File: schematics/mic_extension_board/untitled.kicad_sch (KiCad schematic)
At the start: 10 parts, among them J9 Conn_01x03_Female, U10 LM4881M/NOPB

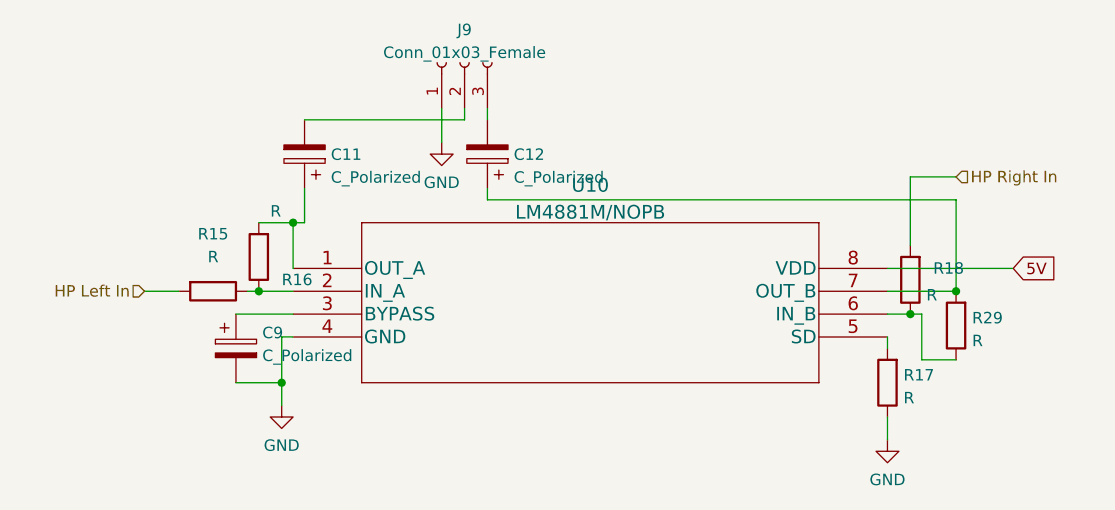
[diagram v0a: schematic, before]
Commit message: re-added component values previously lost due to kicad mishap
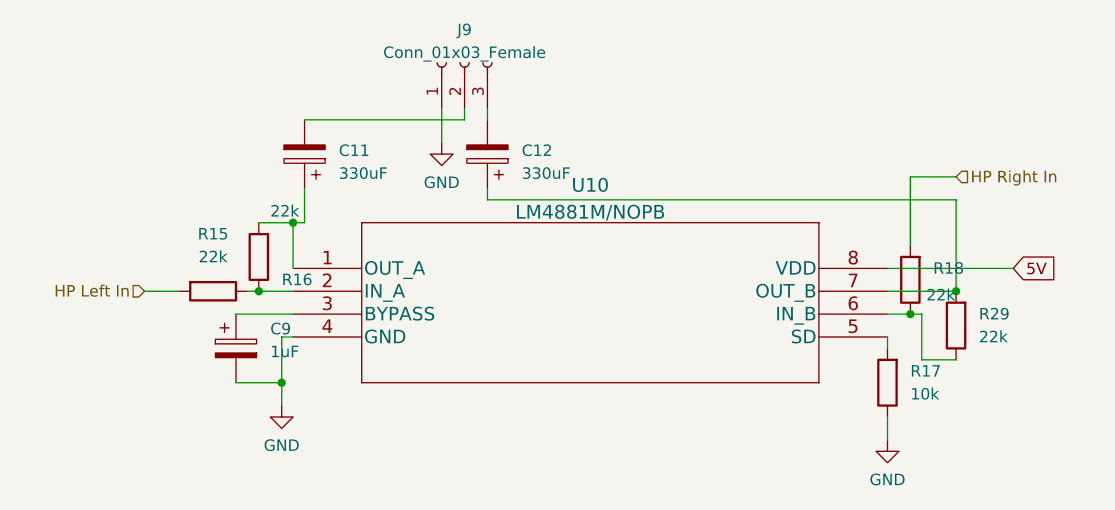
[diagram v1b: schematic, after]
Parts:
- C11, C12: value C_Polarized -> 330uF
- C9: value C_Polarized -> 1uF
- R15, R16, R18, R29: value R -> 22k
- R17: value R -> 10k
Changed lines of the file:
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@@
       (effects (font (size 1.27 1.27)))
     )
-    (property "Value" "R" (at 95.25 55.88 90)
+    (property "Value" "22k" (at 95.25 55.88 90)
       (effects (font (size 1.27 1.27)))
     )
@@
       (effects (font (size 1.27 1.27)) (justify right))
     )
-    (property "Value" "R" (at 174.498 60.1222 0)
+    (property "Value" "22k" (at 174.498 60.1222 0)
       (effects (font (size 1.27 1.27)) (justify right))
     )
@@
       (effects (font (size 1.27 1.27)) (justify right))
     )
-    (property "Value" "R" (at 101.6 50.8 0)
+    (property "Value" "22k" (at 101.6 50.8 0)
       (effects (font (size 1.27 1.27)) (justify right))
     )
@@
   (symbol (lib_id "Device:R") (at 170.18 69.85 180) (unit 1)
     (in_bom yes) (on_board yes) (dnp no) (fields_autoplaced)
-    (property "Reference" "R17" (at 171.958 69.0153 0)
-      (effects (font (size 1.27 1.27)) (justify right))
-    )
-    (property "Value" "R" (at 171.958 71.5522 0)
+    (property "Reference" "R17" (at 172.72 68.58 0)
+      (effects (font (size 1.27 1.27)) (justify right))
+    )
+    (property "Value" "10k" (at 172.72 71.12 0)
       (effects (font (size 1.27 1.27)) (justify right))
     )
@@
   (symbol (lib_id "Device:C_Polarized") (at 105.41 44.45 180) (unit 1)
     (in_bom yes) (on_board yes) (dnp no) (fields_autoplaced)
-    (property "Reference" "C11" (at 108.331 44.5043 0)
-      (effects (font (size 1.27 1.27)) (justify right))
-    )
-    (property "Value" "C_Polarized" (at 108.331 47.0412 0)
+    (property "Reference" "C11" (at 109.22 44.069 0)
+      (effects (font (size 1.27 1.27)) (justify right))
+    )
+    (property "Value" "330uF" (at 109.22 46.609 0)
       (effects (font (size 1.27 1.27)) (justify right))
     )
@@
   (symbol (lib_id "Device:C_Polarized") (at 125.73 44.45 180) (unit 1)
     (in_bom yes) (on_board yes) (dnp no) (fields_autoplaced)
-    (property "Reference" "C12" (at 128.651 44.5043 0)
-      (effects (font (size 1.27 1.27)) (justify right))
-    )
-    (property "Value" "C_Polarized" (at 128.651 47.0412 0)
+    (property "Reference" "C12" (at 129.54 44.069 0)
+      (effects (font (size 1.27 1.27)) (justify right))
+    )
+    (property "Value" "330uF" (at 129.54 46.609 0)
       (effects (font (size 1.27 1.27)) (justify right))
     )
@@
   (symbol (lib_id "Device:C_Polarized") (at 97.79 66.04 0) (unit 1)
     (in_bom yes) (on_board yes) (dnp no) (fields_autoplaced)
-    (property "Reference" "C9" (at 100.711 64.3163 0)
+    (property "Reference" "C9" (at 101.6 63.881 0)
       (effects (font (size 1.27 1.27)) (justify left))
     )
-    (property "Value" "C_Polarized" (at 100.711 66.8532 0)
+    (property "Value" "1uF" (at 101.6 66.421 0)
       (effects (font (size 1.27 1.27)) (justify left))
     )
@@
   (symbol (lib_id "Device:R") (at 177.8 63.5 180) (unit 1)
     (in_bom yes) (on_board yes) (dnp no) (fields_autoplaced)
-    (property "Reference" "R29" (at 179.578 62.6653 0)
-      (effects (font (size 1.27 1.27)) (justify right))
-    )
-    (property "Value" "R" (at 179.578 65.2022 0)
-      (effects (font (size 1.27 1.27)) (justify right))
-    )
+    (property "Reference" "R29" (at 180.34 62.23 0)
+      (effects (font (size 1.27 1.27)) (justify right))
+    )
+    (property "Value" "22k" (at 180.34 64.77 0)
+      (effects (font (size 1.27 1.27)) (justify right))
+    )

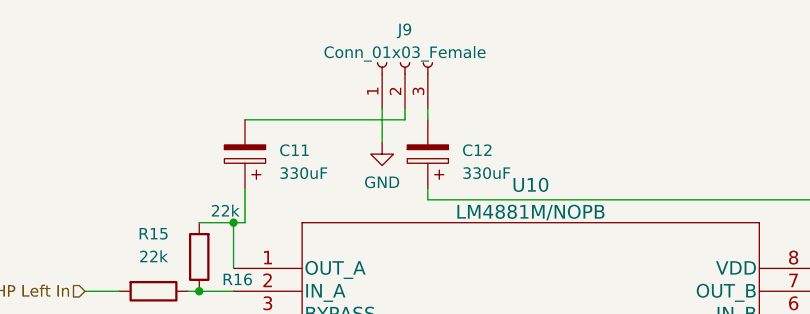
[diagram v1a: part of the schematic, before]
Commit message: fixed layout error, added copper fill
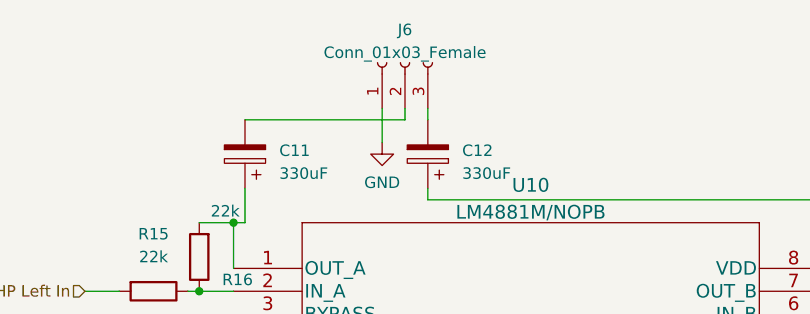
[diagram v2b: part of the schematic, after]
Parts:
- renumbered J9 to J6
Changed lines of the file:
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@@
     (instances
       (project "mic_extension_board"
-        (path "/e63e39d7-6ac0-4ffd-8aa3-1841a4541b55"
-          (reference "R15") (unit 1)
-        )
         (path "/e63e39d7-6ac0-4ffd-8aa3-1841a4541b55/5b76a2fc-3494-4cf0-b601-f44157bc070a"
           (reference "R15") (unit 1)
@@
     (instances
       (project "mic_extension_board"
-        (path "/e63e39d7-6ac0-4ffd-8aa3-1841a4541b55"
-          (reference "U10") (unit 1)
-        )
         (path "/e63e39d7-6ac0-4ffd-8aa3-1841a4541b55/5b76a2fc-3494-4cf0-b601-f44157bc070a"
           (reference "U10") (unit 1)
@@
     (instances
       (project "mic_extension_board"
-        (path "/e63e39d7-6ac0-4ffd-8aa3-1841a4541b55"
-          (reference "R18") (unit 1)
-        )
         (path "/e63e39d7-6ac0-4ffd-8aa3-1841a4541b55/5b76a2fc-3494-4cf0-b601-f44157bc070a"
           (reference "R18") (unit 1)
@@
     (instances
       (project "mic_extension_board"
-        (path "/e63e39d7-6ac0-4ffd-8aa3-1841a4541b55"
+        (path "/e63e39d7-6ac0-4ffd-8aa3-1841a4541b55/5b76a2fc-3494-4cf0-b601-f44157bc070a"
           (reference "R16") (unit 1)
         )
-        (path "/e63e39d7-6ac0-4ffd-8aa3-1841a4541b55/5b76a2fc-3494-4cf0-b601-f44157bc070a"
-          (reference "R16") (unit 1)
-        )
       )
     )
@@
     (instances
       (project "mic_extension_board"
-        (path "/e63e39d7-6ac0-4ffd-8aa3-1841a4541b55"
+        (path "/e63e39d7-6ac0-4ffd-8aa3-1841a4541b55/5b76a2fc-3494-4cf0-b601-f44157bc070a"
           (reference "#PWR016") (unit 1)
         )
-        (path "/e63e39d7-6ac0-4ffd-8aa3-1841a4541b55/5b76a2fc-3494-4cf0-b601-f44157bc070a"
-          (reference "#PWR016") (unit 1)
-        )
       )
     )
@@
   (symbol (lib_id "power:GND") (at 170.18 76.2 0) (unit 1)
     (in_bom yes) (on_board yes) (dnp no) (fields_autoplaced)
-    (property "Reference" "#PWR018" (at 170.18 82.55 0)
+    (property "Reference" "#PWR024" (at 170.18 82.55 0)
       (effects (font (size 1.27 1.27)) hide)
     )
@@
     (instances
       (project "mic_extension_board"
-        (path "/e63e39d7-6ac0-4ffd-8aa3-1841a4541b55"
+        (path "/e63e39d7-6ac0-4ffd-8aa3-1841a4541b55/5b76a2fc-3494-4cf0-b601-f44157bc070a"
+          (reference "#PWR024") (unit 1)
+        )
+      )
+    )
+  )
+  (symbol (lib_id "power:GND") (at 120.65 43.18 0) (unit 1)
+    (in_bom yes) (on_board yes) (dnp no) (fields_autoplaced)
+    (property "Reference" "#PWR018" (at 120.65 49.53 0)
+      (effects (font (size 1.27 1.27)) hide)
+    )
+    (property "Value" "GND" (at 120.65 47.6234 0)
+      (effects (font (size 1.27 1.27)))
+    )
+    (property "Footprint" "" (at 120.65 43.18 0)
+      (effects (font (size 1.27 1.27)) hide)
+    )
+    (property "Datasheet" "" (at 120.65 43.18 0)
+      (effects (font (size 1.27 1.27)) hide)
+    )
+    (pin "1")
+    (instances
+      (project "mic_extension_board"
+        (path "/e63e39d7-6ac0-4ffd-8aa3-1841a4541b55/5b76a2fc-3494-4cf0-b601-f44157bc070a"
           (reference "#PWR018") (unit 1)
         )
-        (path "/e63e39d7-6ac0-4ffd-8aa3-1841a4541b55/5b76a2fc-3494-4cf0-b601-f44157bc070a"
-          (reference "#PWR024") (unit 1)
-        )
-      )
-    )
-  )
-  (symbol (lib_id "power:GND") (at 120.65 43.18 0) (unit 1)
-    (in_bom yes) (on_board yes) (dnp no) (fields_autoplaced)
-    (property "Reference" "#PWR024" (at 120.65 49.53 0)
-      (effects (font (size 1.27 1.27)) hide)
-    )
-    (property "Value" "GND" (at 120.65 47.6234 0)
-      (effects (font (size 1.27 1.27)))
-    )
-    (property "Footprint" "" (at 120.65 43.18 0)
-      (effects (font (size 1.27 1.27)) hide)
-    )
-    (property "Datasheet" "" (at 120.65 43.18 0)
-      (effects (font (size 1.27 1.27)) hide)
-    )
-    (pin "1")
-    (instances
-      (project "mic_extension_board"
-        (path "/e63e39d7-6ac0-4ffd-8aa3-1841a4541b55"
-          (reference "#PWR024") (unit 1)
-        )
-        (path "/e63e39d7-6ac0-4ffd-8aa3-1841a4541b55/5b76a2fc-3494-4cf0-b601-f44157bc070a"
-          (reference "#PWR018") (unit 1)
-        )
       )
     )
@@
     (instances
       (project "mic_extension_board"
-        (path "/e63e39d7-6ac0-4ffd-8aa3-1841a4541b55"
+        (path "/e63e39d7-6ac0-4ffd-8aa3-1841a4541b55/5b76a2fc-3494-4cf0-b601-f44157bc070a"
           (reference "R17") (unit 1)
         )
-        (path "/e63e39d7-6ac0-4ffd-8aa3-1841a4541b55/5b76a2fc-3494-4cf0-b601-f44157bc070a"
-          (reference "R17") (unit 1)
-        )
       )
     )
@@
   (symbol (lib_id "Connector:Conn_01x03_Female") (at 123.19 34.29 90) (unit 1)
     (in_bom yes) (on_board yes) (dnp no) (fields_autoplaced)
-    (property "Reference" "J9" (at 123.19 30.641 90)
+    (property "Reference" "J6" (at 123.19 30.641 90)
       (effects (font (size 1.27 1.27)))
     )
@@
     (instances
       (project "mic_extension_board"
-        (path "/e63e39d7-6ac0-4ffd-8aa3-1841a4541b55"
-          (reference "J9") (unit 1)
-        )
         (path "/e63e39d7-6ac0-4ffd-8aa3-1841a4541b55/5b76a2fc-3494-4cf0-b601-f44157bc070a"
           (reference "J6") (unit 1)
@@
     (instances
       (project "mic_extension_board"
-        (path "/e63e39d7-6ac0-4ffd-8aa3-1841a4541b55"
+        (path "/e63e39d7-6ac0-4ffd-8aa3-1841a4541b55/5b76a2fc-3494-4cf0-b601-f44157bc070a"
           (reference "C11") (unit 1)
         )
-        (path "/e63e39d7-6ac0-4ffd-8aa3-1841a4541b55/5b76a2fc-3494-4cf0-b601-f44157bc070a"
-          (reference "C11") (unit 1)
-        )
       )
     )
@@
     (instances
       (project "mic_extension_board"
-        (path "/e63e39d7-6ac0-4ffd-8aa3-1841a4541b55"
-          (reference "C12") (unit 1)
-        )
         (path "/e63e39d7-6ac0-4ffd-8aa3-1841a4541b55/5b76a2fc-3494-4cf0-b601-f44157bc070a"
           (reference "C12") (unit 1)
@@
     (instances
       (project "mic_extension_board"
-        (path "/e63e39d7-6ac0-4ffd-8aa3-1841a4541b55"
+        (path "/e63e39d7-6ac0-4ffd-8aa3-1841a4541b55/5b76a2fc-3494-4cf0-b601-f44157bc070a"
           (reference "C9") (unit 1)
         )
-        (path "/e63e39d7-6ac0-4ffd-8aa3-1841a4541b55/5b76a2fc-3494-4cf0-b601-f44157bc070a"
-          (reference "C9") (unit 1)
-        )
       )
     )
@@
     (instances
       (project "mic_extension_board"
-        (path "/e63e39d7-6ac0-4ffd-8aa3-1841a4541b55"
+        (path "/e63e39d7-6ac0-4ffd-8aa3-1841a4541b55/5b76a2fc-3494-4cf0-b601-f44157bc070a"
           (reference "R29") (unit 1)
-        )
-        (path "/e63e39d7-6ac0-4ffd-8aa3-1841a4541b55/5b76a2fc-3494-4cf0-b601-f44157bc070a"
-          (reference "R29") (unit 1)
